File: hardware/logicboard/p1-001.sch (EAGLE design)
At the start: 24 parts, among them IC1 74LS07N

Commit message: OSHW logo.
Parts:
- added LOGO2: OSHW-LOGOL-COPPER, SparkFun-Aesthetics:OSHW-LOGOL-COPPER
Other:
- note added: "Pineapple I 1.0.1"
- note removed: "Pineapple I 1.0.0 by Pineapple Design"
- moved on the sheet: ANALOG, C1, C2, C3, D1, FRONT, I2C, IC1A, IC1B, IC1C, IC1D, IC1E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

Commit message: Pineapple logo v2.
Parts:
- removed LOGO2: OSHW-LOGOL-COPPER, SparkFun-Aesthetics:OSHW-LOGOL-COPPER
- added LOGO1: OSHW-LOGOS-COPPER, SparkFun-Aesthetics:OSHW-LOGOS-COPPER
- added U$2: PINEAPPLELOGO2, pineapplelogo2:PINEAPPLELOGO2
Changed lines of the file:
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@@
 <part name="RSV" library="SparkFun-Connectors" library_urn="urn:adsk.eagle:library:513" deviceset="CONN_05" device="1.27MM" package3d_urn="urn:adsk.eagle:package:38110/1"/>
 <part name="FRAME1" library="frames" library_urn="urn:adsk.eagle:library:229" deviceset="A4L-LOC" device=""/>
-<part name="LOGO2" library="SparkFun-Aesthetics" deviceset="OSHW-LOGO" device="L-COPPER"/>
+<part name="LOGO1" library="SparkFun-Aesthetics" deviceset="OSHW-LOGO" device="S-COPPER"/>
+<part name="U$2" library="pineapplelogo2" deviceset="PINEAPPLELOGO2" device=""/>
 </parts>
 <sheets>
@@
 <instance part="RSV" gate="G$1" x="139.7" y="78.74" rot="R180"/>
 <instance part="FRAME1" gate="G$1" x="0" y="0"/>
-<instance part="LOGO2" gate="G$1" x="200.66" y="15.24"/>
+<instance part="LOGO1" gate="G$1" x="241.3" y="165.1"/>
+<instance part="U$2" gate="G$1" x="187.96" y="7.62"/>
 </instances>
 <busses>

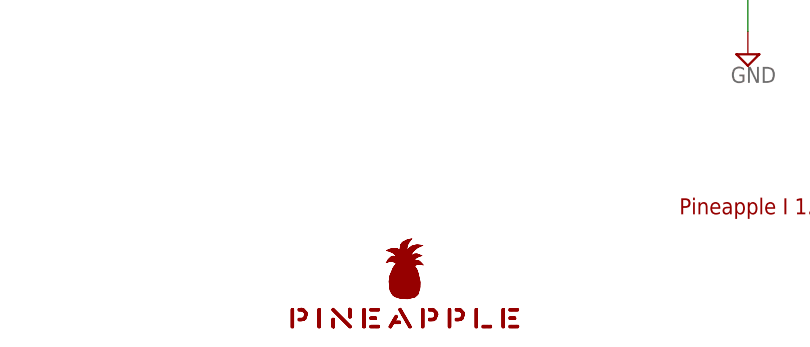
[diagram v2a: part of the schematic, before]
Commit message: New pineapple logo.
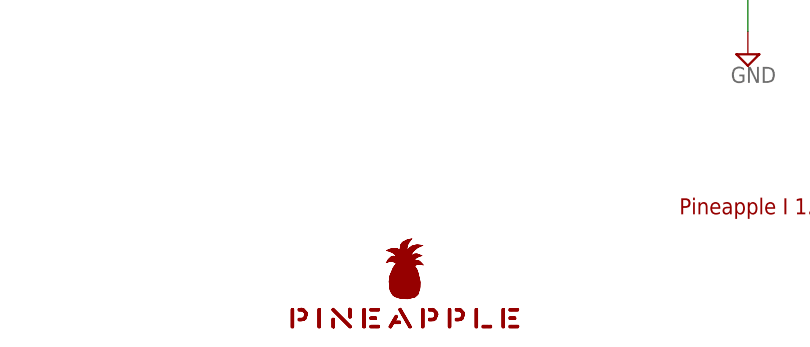
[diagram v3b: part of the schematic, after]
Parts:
- LOGO1: value OSHW-LOGOS-COPPER -> OSHW-LOGOS; device SparkFun-Aesthetics:OSHW-LOGOS-COPPER -> SparkFun-Aesthetics:OSHW-LOGOS
- U$2: value PINEAPPLELOGO2 -> PINEAPPLELOGO2SILKMINI; device pineapplelogo2:PINEAPPLELOGO2 -> pineapplelogo:PINEAPPLELOGO2SILKMINI
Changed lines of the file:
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@@
 <part name="RSV" library="SparkFun-Connectors" library_urn="urn:adsk.eagle:library:513" deviceset="CONN_05" device="1.27MM" package3d_urn="urn:adsk.eagle:package:38110/1"/>
 <part name="FRAME1" library="frames" library_urn="urn:adsk.eagle:library:229" deviceset="A4L-LOC" device=""/>
-<part name="LOGO1" library="SparkFun-Aesthetics" deviceset="OSHW-LOGO" device="S-COPPER"/>
-<part name="U$2" library="pineapplelogo2" deviceset="PINEAPPLELOGO2" device=""/>
+<part name="LOGO1" library="SparkFun-Aesthetics" deviceset="OSHW-LOGO" device="S" value="OSHW-LOGOS"/>
+<part name="U$2" library="pineapplelogo" deviceset="PINEAPPLELOGO2SILKMINI" device=""/>
 </parts>
 <sheets>

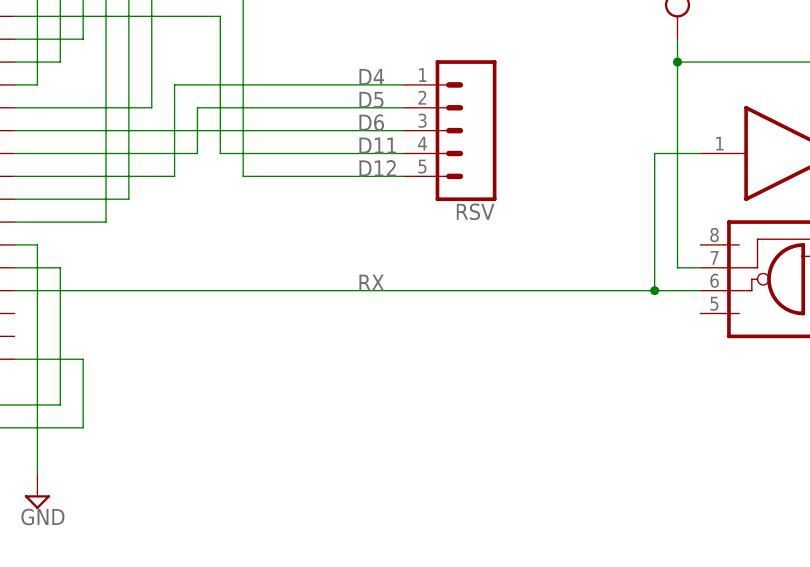
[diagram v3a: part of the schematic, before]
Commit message: Changed signal names.
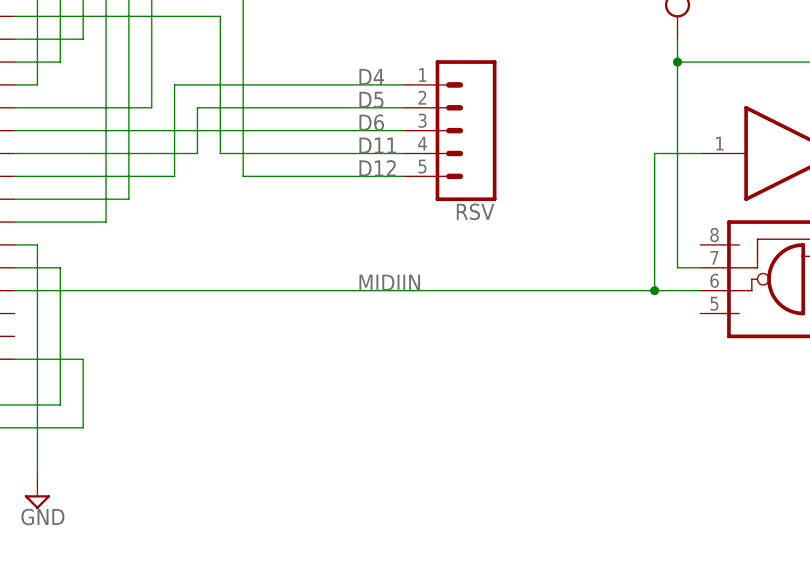
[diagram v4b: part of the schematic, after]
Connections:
- net N$10 renamed A1
- net N$11 renamed A2
- net N$12 renamed A3
- net N$13 renamed A4
- net N$14 renamed A5
- net N$2 renamed N$MIDITHRU-RAW
- net N$3 renamed INDR
- net N$5 renamed MIDIINA
- net N$9 renamed A0
- net RX renamed MIDIIN
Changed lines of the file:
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@@
 </segment>
 </net>
-<net name="N$2" class="0">
+<net name="N$MIDITHRU-RAW" class="0">
 <segment>
 <pinref part="IC1" gate="A" pin="O"/>
@@
 </segment>
 </net>
-<net name="RX" class="0">
+<net name="MIDIIN" class="0">
 <segment>
 <pinref part="OK1" gate="A" pin="VO"/>
@@
 </segment>
 </net>
-<net name="N$5" class="0">
+<net name="MIDIINA" class="0">
 <segment>
 <pinref part="OK1" gate="A" pin="A"/>
@@
 </segment>
 </net>
-<net name="N$3" class="0">
+<net name="INDR" class="0">
 <segment>
 <pinref part="R1" gate="G$1" pin="1"/>
@@
 </segment>
 </net>
-<net name="N$9" class="0">
+<net name="A0" class="0">
 <segment>
 <pinref part="U$1" gate="G$1" pin="A0"/>
@@
 </segment>
 </net>
-<net name="N$10" class="0">
+<net name="A1" class="0">
 <segment>
 <pinref part="U$1" gate="G$1" pin="A1"/>
@@
 </segment>
 </net>
-<net name="N$11" class="0">
+<net name="A2" class="0">
 <segment>
 <pinref part="U$1" gate="G$1" pin="A2"/>
@@
 </segment>
 </net>
-<net name="N$12" class="0">
+<net name="A3" class="0">
 <segment>
 <pinref part="U$1" gate="G$1" pin="A3"/>
@@
 </segment>
 </net>
-<net name="N$13" class="0">
+<net name="A4" class="0">
 <segment>
 <pinref part="U$1" gate="G$1" pin="A4"/>
@@
 </segment>
 </net>
-<net name="N$14" class="0">
+<net name="A5" class="0">
 <segment>
 <pinref part="U$1" gate="G$1" pin="A5"/>

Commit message: Version 1.0.1 -> 1.2.0.
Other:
- note added: "Pineapple I 1.2.0"
- note removed: "Pineapple I 1.0.1"
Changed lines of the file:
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@@
 <sheet>
 <plain>
-<text x="218.44" y="20.32" size="1.778" layer="94">Pineapple I 1.0.1</text>
+<text x="218.44" y="20.32" size="1.778" layer="94">Pineapple I 1.2.0</text>
 </plain>
 <instances>

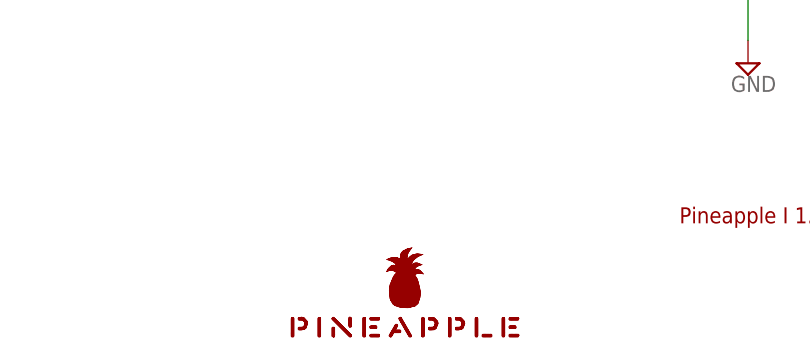
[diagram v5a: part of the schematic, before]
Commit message: Pineapple Logo (vector->bitmap), OSHW logo (silk -> copper).
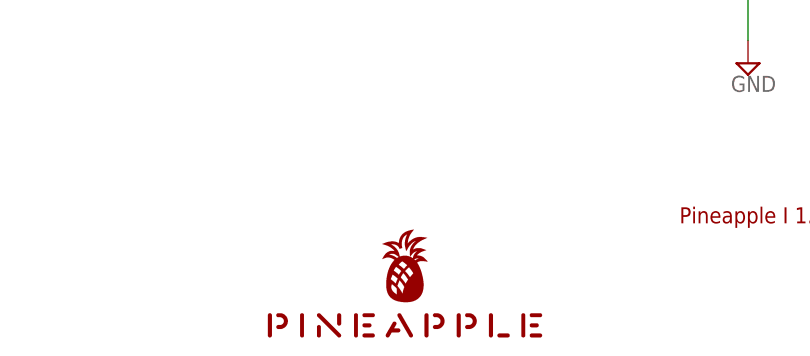
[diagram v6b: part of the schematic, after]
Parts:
- LOGO1: value OSHW-LOGOS -> OSHW-LOGOS-COPPER; device SparkFun-Aesthetics:OSHW-LOGOS -> SparkFun-Aesthetics:OSHW-LOGOS-COPPER
- U$2: value PINEAPPLELOGO2SILKMINI -> PINEAPPLE450; device pineapplelogo:PINEAPPLELOGO2SILKMINI -> pineapple:PINEAPPLE450
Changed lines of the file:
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@@
 <part name="RSV" library="SparkFun-Connectors" library_urn="urn:adsk.eagle:library:513" deviceset="CONN_05" device="1.27MM" package3d_urn="urn:adsk.eagle:package:38110/1"/>
 <part name="FRAME1" library="frames" library_urn="urn:adsk.eagle:library:229" deviceset="A4L-LOC" device=""/>
-<part name="LOGO1" library="SparkFun-Aesthetics" deviceset="OSHW-LOGO" device="S" value="OSHW-LOGOS"/>
-<part name="U$2" library="pineapplelogo" deviceset="PINEAPPLELOGO2SILKMINI" device=""/>
+<part name="LOGO1" library="SparkFun-Aesthetics" deviceset="OSHW-LOGO" device="S-COPPER" value="OSHW-LOGOS-COPPER"/>
+<part name="U$2" library="pineapple" deviceset="PINEAPPLE450" device=""/>
 </parts>
 <sheets>

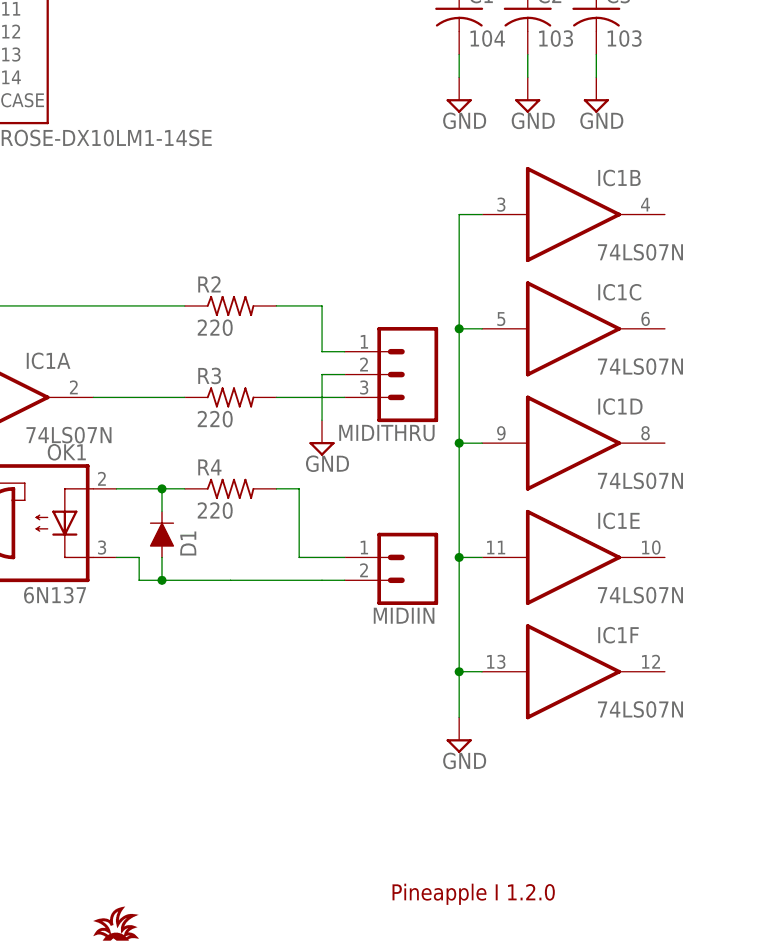
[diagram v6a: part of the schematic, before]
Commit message: Unified MIDI connector.
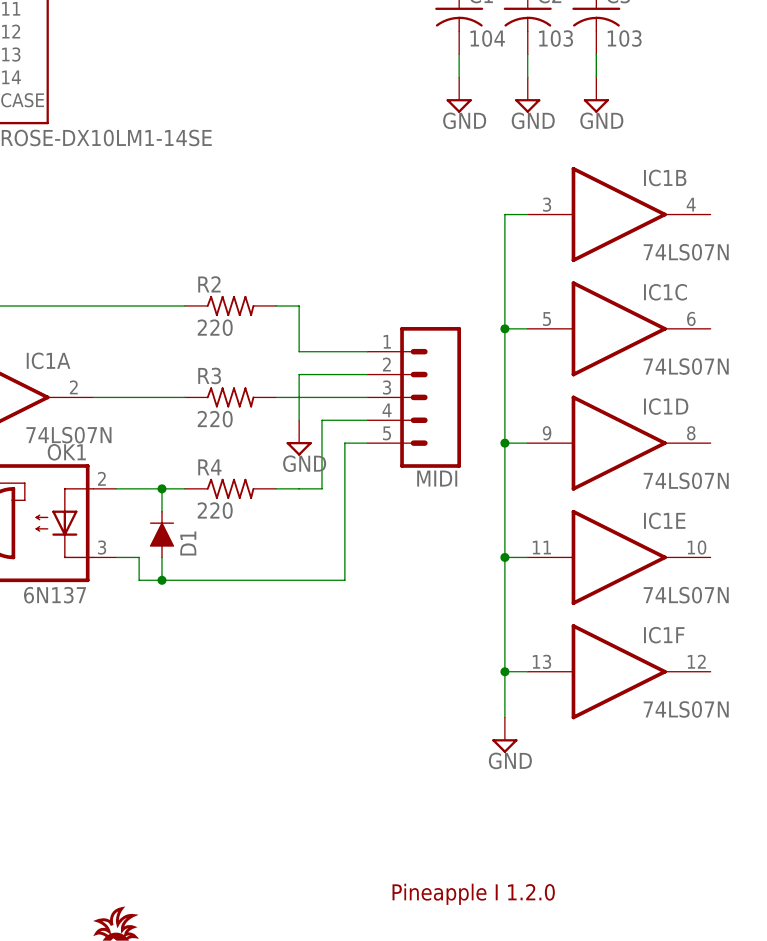
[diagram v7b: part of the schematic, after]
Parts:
- removed MIDIIN: (no value), SparkFun-Connectors:CONN_02JST-PTH-2
- removed MIDITHRU: (no value), SparkFun-Connectors:CONN_03JST-PTH
- added MIDI: (no value), SparkFun-Connectors:CONN_05JST
- U$2: value PINEAPPLE450 -> PINEAPPLE450_SILK; device pineapple:PINEAPPLE450 -> pineapple:PINEAPPLE450_SILK
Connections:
- net GND: now also MIDI.2; no longer MIDITHRU.2
- net MIDIIN+: now also MIDI.4; no longer MIDIIN.1
- net MIDIIN-: now also MIDI.5; no longer MIDIIN.2
- net MIDITHRU+: now also MIDI.1; no longer MIDITHRU.1
- net MIDITHRU-: now also MIDI.3; no longer MIDITHRU.3
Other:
- moved on the sheet: IC1B, IC1C, IC1D, IC1E, IC1F
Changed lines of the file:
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@@
 <part name="SUPPLY14" library="supply2" library_urn="urn:adsk.eagle:library:372" deviceset="VCC" device=""/>
 <part name="$1_39_$_2018-07-15_07-03-06" library="supply2" library_urn="urn:adsk.eagle:library:372" deviceset="GND" device=""/>
-<part name="MIDIIN" library="SparkFun-Connectors" deviceset="CONN_02" device="JST-PTH-2"/>
-<part name="MIDITHRU" library="SparkFun-Connectors" deviceset="CONN_03" device="JST-PTH"/>
 <part name="$1_53_$_2018-07-15_07-03-06" library="supply2" library_urn="urn:adsk.eagle:library:372" deviceset="GND" device=""/>
 <part name="PWMDRV" library="SparkFun-Retired" deviceset="TLC5940" device="-NT"/>
@@
 <part name="FRAME1" library="frames" library_urn="urn:adsk.eagle:library:229" deviceset="A4L-LOC" device=""/>
 <part name="LOGO1" library="SparkFun-Aesthetics" deviceset="OSHW-LOGO" device="S-COPPER" value="OSHW-LOGOS-COPPER"/>
-<part name="U$2" library="pineapple" deviceset="PINEAPPLE450" device=""/>
+<part name="U$2" library="pineapple" deviceset="PINEAPPLE450_SILK" device=""/>
+<part name="MIDI" library="SparkFun-Connectors" library_urn="urn:adsk.eagle:library:513" deviceset="CONN_05" device="JST" package3d_urn="urn:adsk.eagle:package:38120/1"/>
 </parts>
 <sheets>
@@
 <instance part="C2" gate="G$1" x="233.68" y="119.38"/>
 <instance part="C3" gate="G$1" x="241.3" y="119.38"/>
-<instance part="IC1" gate="D" x="238.76" y="71.12"/>
-<instance part="IC1" gate="E" x="238.76" y="58.42"/>
-<instance part="IC1" gate="F" x="238.76" y="45.72"/>
-<instance part="$1_55_$_2018-07-15_07-03-06" gate="GND" x="226.06" y="38.1"/>
-<instance part="IC1" gate="B" x="238.76" y="96.52"/>
-<instance part="IC1" gate="C" x="238.76" y="83.82"/>
+<instance part="IC1" gate="D" x="243.84" y="71.12"/>
+<instance part="IC1" gate="E" x="243.84" y="58.42"/>
+<instance part="IC1" gate="F" x="243.84" y="45.72"/>
+<instance part="$1_55_$_2018-07-15_07-03-06" gate="GND" x="231.14" y="38.1"/>
+<instance part="IC1" gate="B" x="243.84" y="96.52"/>
+<instance part="IC1" gate="C" x="243.84" y="83.82"/>
 <instance part="D1" gate="G$1" x="193.04" y="60.96" rot="MR90"/>
 <instance part="SUPPLY14" gate="G$1" x="25.4" y="71.12"/>
 <instance part="$1_39_$_2018-07-15_07-03-06" gate="GND" x="60.96" y="38.1"/>
-<instance part="MIDIIN" gate="G$1" x="220.98" y="58.42" rot="R180"/>
-<instance part="MIDITHRU" gate="J$1" x="220.98" y="78.74" rot="R180"/>
-<instance part="$1_53_$_2018-07-15_07-03-06" gate="GND" x="210.82" y="71.12"/>
+<instance part="$1_53_$_2018-07-15_07-03-06" gate="GND" x="208.28" y="71.12"/>
 <instance part="PWMDRV" gate="G$1" x="88.9" y="137.16" rot="R90"/>
 <instance part="$1_43_$_2018-07-15_07-03-06" gate="GND" x="109.22" y="119.38"/>
@@
 <instance part="LOGO1" gate="G$1" x="241.3" y="165.1"/>
 <instance part="U$2" gate="G$1" x="187.96" y="7.62"/>
+<instance part="MIDI" gate="G$1" x="223.52" y="76.2" rot="R180"/>
 </instances>
 <busses>
@@
 <pinref part="$1_55_$_2018-07-15_07-03-06" gate="GND" pin="GND"/>
 <pinref part="IC1" gate="F" pin="I"/>
-<wire x1="226.06" y1="58.42" x2="226.06" y2="45.72" width="0.1524" layer="91"/>
-<wire x1="226.06" y1="45.72" x2="226.06" y2="40.64" width="0.1524" layer="91"/>
-<wire x1="228.6" y1="45.72" x2="226.06" y2="45.72" width="0.1524" layer="91"/>
+<wire x1="231.14" y1="58.42" x2="231.14" y2="45.72" width="0.1524" layer="91"/>
+<wire x1="231.14" y1="45.72" x2="231.14" y2="40.64" width="0.1524" layer="91"/>
+<wire x1="233.68" y1="45.72" x2="231.14" y2="45.72" width="0.1524" layer="91"/>
 <pinref part="IC1" gate="E" pin="I"/>
-<wire x1="228.6" y1="58.42" x2="226.06" y2="58.42" width="0.1524" layer="91"/>
-<junction x="226.06" y="45.72"/>
+<wire x1="233.68" y1="58.42" x2="231.14" y2="58.42" width="0.1524" layer="91"/>
+<junction x="231.14" y="45.72"/>
 <pinref part="IC1" gate="B" pin="I"/>
-<wire x1="228.6" y1="96.52" x2="226.06" y2="96.52" width="0.1524" layer="91"/>
-<wire x1="226.06" y1="96.52" x2="226.06" y2="83.82" width="0.1524" layer="91"/>
-<junction x="226.06" y="58.42"/>
+<wire x1="233.68" y1="96.52" x2="231.14" y2="96.52" width="0.1524" layer="91"/>
+<wire x1="231.14" y1="96.52" x2="231.14" y2="83.82" width="0.1524" layer="91"/>
+<junction x="231.14" y="58.42"/>
 <pinref part="IC1" gate="C" pin="I"/>
-<wire x1="226.06" y1="83.82" x2="226.06" y2="71.12" width="0.1524" layer="91"/>
-<wire x1="226.06" y1="71.12" x2="226.06" y2="58.42" width="0.1524" layer="91"/>
-<wire x1="228.6" y1="83.82" x2="226.06" y2="83.82" width="0.1524" layer="91"/>
-<junction x="226.06" y="83.82"/>
+<wire x1="231.14" y1="83.82" x2="231.14" y2="71.12" width="0.1524" layer="91"/>
+<wire x1="231.14" y1="71.12" x2="231.14" y2="58.42" width="0.1524" layer="91"/>
+<wire x1="233.68" y1="83.82" x2="231.14" y2="83.82" width="0.1524" layer="91"/>
+<junction x="231.14" y="83.82"/>
 <pinref part="IC1" gate="D" pin="I"/>
-<wire x1="228.6" y1="71.12" x2="226.06" y2="71.12" width="0.1524" layer="91"/>
-<junction x="226.06" y="71.12"/>
+<wire x1="233.68" y1="71.12" x2="231.14" y2="71.12" width="0.1524" layer="91"/>
+<junction x="231.14" y="71.12"/>
 </segment>
 <segment>
@@
 </segment>
 <segment>
-<pinref part="MIDITHRU" gate="J$1" pin="2"/>
 <pinref part="$1_53_$_2018-07-15_07-03-06" gate="GND" pin="GND"/>
-<wire x1="213.36" y1="78.74" x2="210.82" y2="78.74" width="0.1524" layer="91"/>
-<wire x1="210.82" y1="78.74" x2="210.82" y2="73.66" width="0.1524" layer="91"/>
+<wire x1="215.9" y1="78.74" x2="208.28" y2="78.74" width="0.1524" layer="91"/>
+<wire x1="208.28" y1="78.74" x2="208.28" y2="73.66" width="0.1524" layer="91"/>
+<pinref part="MIDI" gate="G$1" pin="2"/>
 </segment>
 <segment>
@@
 <net name="MIDITHRU-" class="0">
 <segment>
-<wire x1="205.74" y1="76.2" x2="213.36" y2="76.2" width="0.1524" layer="91"/>
-<pinref part="MIDITHRU" gate="J$1" pin="3"/>
+<wire x1="205.74" y1="76.2" x2="215.9" y2="76.2" width="0.1524" layer="91"/>
 <pinref part="R3" gate="G$1" pin="2"/>
+<pinref part="MIDI" gate="G$1" pin="3"/>
 </segment>
 </net>
@@
 <wire x1="190.5" y1="58.42" x2="190.5" y2="55.88" width="0.1524" layer="91"/>
 <wire x1="190.5" y1="55.88" x2="193.04" y2="55.88" width="0.1524" layer="91"/>
-<wire x1="193.04" y1="55.88" x2="200.66" y2="55.88" width="0.1524" layer="91"/>
-<wire x1="200.66" y1="55.88" x2="210.82" y2="55.88" width="0.1524" layer="91"/>
-<wire x1="210.82" y1="55.88" x2="213.36" y2="55.88" width="0.1524" layer="91"/>
-<pinref part="MIDIIN" gate="G$1" pin="2"/>
 <pinref part="D1" gate="G$1" pin="A"/>
 <wire x1="193.04" y1="58.42" x2="193.04" y2="55.88" width="0.1524" layer="91"/>
+<pinref part="MIDI" gate="G$1" pin="5"/>
+<wire x1="215.9" y1="71.12" x2="213.36" y2="71.12" width="0.1524" layer="91"/>
+<wire x1="213.36" y1="71.12" x2="213.36" y2="55.88" width="0.1524" layer="91"/>
+<wire x1="213.36" y1="55.88" x2="193.04" y2="55.88" width="0.1524" layer="91"/>
 <junction x="193.04" y="55.88"/>
 </segment>
@@
 <segment>
 <wire x1="205.74" y1="66.04" x2="208.28" y2="66.04" width="0.1524" layer="91"/>
-<wire x1="208.28" y1="66.04" x2="208.28" y2="58.42" width="0.1524" layer="91"/>
-<pinref part="MIDIIN" gate="G$1" pin="1"/>
-<wire x1="208.28" y1="58.42" x2="213.36" y2="58.42" width="0.1524" layer="91"/>
 <pinref part="R4" gate="G$1" pin="2"/>
+<pinref part="MIDI" gate="G$1" pin="4"/>
+<wire x1="215.9" y1="73.66" x2="210.82" y2="73.66" width="0.1524" layer="91"/>
+<wire x1="210.82" y1="73.66" x2="210.82" y2="66.04" width="0.1524" layer="91"/>
+<wire x1="210.82" y1="66.04" x2="208.28" y2="66.04" width="0.1524" layer="91"/>
 </segment>
 </net>
 <net name="MIDITHRU+" class="0">
 <segment>
-<wire x1="205.74" y1="86.36" x2="210.82" y2="86.36" width="0.1524" layer="91"/>
-<wire x1="210.82" y1="86.36" x2="210.82" y2="81.28" width="0.1524" layer="91"/>
-<pinref part="MIDITHRU" gate="J$1" pin="1"/>
-<wire x1="210.82" y1="81.28" x2="213.36" y2="81.28" width="0.1524" layer="91"/>
+<wire x1="205.74" y1="86.36" x2="208.28" y2="86.36" width="0.1524" layer="91"/>
+<wire x1="208.28" y1="86.36" x2="208.28" y2="81.28" width="0.1524" layer="91"/>
+<wire x1="208.28" y1="81.28" x2="215.9" y2="81.28" width="0.1524" layer="91"/>
 <pinref part="R2" gate="G$1" pin="2"/>
-</segment>
-</net>
+<pinref part="MIDI" gate="G$1" pin="1"/>
+</segment>
+</net>
